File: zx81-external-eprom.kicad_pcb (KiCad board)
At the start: 2 copper layers, 60.3 x 50 mm, 11 parts, among them J1 Connector ZX81, Q1 BC549, SW1 ROM select, U1 W27C512, U2 74LS138

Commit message: cosmetic changes
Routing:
- added copper zone on F.Cu, net GND
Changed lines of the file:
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@@
 		)
 		(property "Value" "ROM select"
-			(at 3.77 9.2 270)
+			(at 3.77 9.2 -90)
 			(layer "F.SilkS")
 			(effects
@@
 	)
 	(zone
+		(net 21)
+		(net_name "GND")
+		(layer "F.Cu")
+		(hatch edge 0.5)
+		(connect_pads
+			(clearance 0.5)
+		)
+		(min_thickness 0.25)
+		(filled_areas_thickness no)
+		(fill yes
+			(thermal_gap 0.5)
+			(thermal_bridge_width 0.5)
+		)
+		(polygon
+			(pts
+				(xy 107.45 37.97) (xy 47.71 37.97) (xy 47.71 79.11) (xy 107.46 79.12)
+			)
+		)
+	)
+	(zone

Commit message: Local SYMBOL & FOOTPRINT
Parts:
- G200: footprint ZXINFO:ZXInfo_kicad_logo_copper_16.5x5 -> ZXINFO_FOOTPRINT:ZXInfo_kicad_logo_copper_16.5x5
- J1: footprint ZXINFO:EDGE ZX81_1 -> ZXINFO_FOOTPRINT:EDGE ZX81 BOTTOM
- SW1: value ROM select -> SW_DIP_x03
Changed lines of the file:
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@@
 		)
 	)
-	(footprint "ZXINFO:EDGE ZX81_1"
+	(footprint "ZXINFO_FOOTPRINT:EDGE ZX81 BOTTOM"
 		(layer "F.Cu")
 		(at 78.9246 83.68)
@@
 			)
 		)
-		(property "Footprint" "ZXINFO:EDGE ZX81_1"
+		(property "Footprint" "ZXINFO_FOOTPRINT:EDGE ZX81 BOTTOM"
 			(at -5.104618 2.54 180)
 			(unlocked yes)
@@
 			)
 		)
+		(property ki_fp_filters "SINCLAIR:ZX_*")
+		(sheetname "Root")
+		(sheetfile "zx81-external-eprom.kicad_sch")
 		(attr through_hole)
-		(fp_text user "A0"
-			(at -14.187654 -4.530952 -90)
+		(fp_text user "A9"
+			(at 11.2 -4.530952 -90)
 			(unlocked yes)
 			(layer "B.SilkS")
@@
 			)
 		)
-		(fp_text user "A8"
-			(at 13.762365 -4.530952 -90)
+		(fp_text user "GND"
+			(at -19.237654 -4.530952 -90)
 			(unlocked yes)
 			(layer "B.SilkS")
@@
 			)
 		)
-		(fp_text user "+9V"
-			(at -26.887654 -4.530952 -90)
+		(fp_text user "A10"
+			(at 8.75 -4.530952 -90)
 			(unlocked yes)
 			(layer "B.SilkS")
@@
 			)
 		)
-		(fp_text user "A11"
-			(at 5.962365 -4.530952 -90)
+		(fp_text user "A2"
+			(at -9.137654 -4.530952 -90)
 			(unlocked yes)
 			(layer "B.SilkS")
@@
 			)
 		)
-		(fp_text user "SLOT"
-			(at 19 2.1 90)
+		(fp_text user "CLK"
+			(at -16.687654 -4.530952 -90)
 			(unlocked yes)
 			(layer "B.SilkS")
-			(hide yes)
 			(effects
 				(font
@@
 			)
 		)
-		(fp_text user "A9"
-			(at 11.2 -4.530952 -90)
+		(fp_text user "A15"
+			(at -4.087654 -4.530952 -90)
 			(unlocked yes)
 			(layer "B.SilkS")
@@
 			)
 		)
-		(fp_text user "CLK"
-			(at -16.687654 -4.530952 -90)
+		(fp_text user "A8"
+			(at 13.762365 -4.530952 -90)
 			(unlocked yes)
 			(layer "B.SilkS")
@@
 			)
 		)
-		(fp_text user "A15"
-			(at -4.087654 -4.530952 -90)
+		(fp_text user "SLOT"
+			(at 19 2.1 90)
 			(unlocked yes)
 			(layer "B.SilkS")
+			(hide yes)
 			(effects
 				(font
@@
 			)
 		)
-		(fp_text user "A6"
-			(at 18.741358 -4.530952 -90)
+		(fp_text user "A1"
+			(at -11.587654 -4.530952 -90)
 			(unlocked yes)
 			(layer "B.SilkS")
@@
 			)
 		)
-		(fp_text user "~{ROMCS}"
-			(at 26.65 -4.530952 -90)
+		(fp_text user "A13"
+			(at 0.855556 -4.530952 -90)
 			(unlocked yes)
 			(layer "B.SilkS")
@@
 			)
 		)
-		(fp_text user "A14"
-			(at -1.387654 -4.530952 -90)
+		(fp_text user "A11"
+			(at 5.962365 -4.530952 -90)
 			(unlocked yes)
 			(layer "B.SilkS")
@@
 			)
 		)
-		(fp_text user "A2"
-			(at -9.137654 -4.530952 -90)
+		(fp_text user "A12"
+			(at 3.512365 -4.530952 -90)
 			(unlocked yes)
 			(layer "B.SilkS")
@@
 			)
 		)
-		(fp_text user "A10"
-			(at 8.75 -4.530952 -90)
+		(fp_text user "A7"
+			(at 16.248148 -4.530952 -90)
 			(unlocked yes)
 			(layer "B.SilkS")
@@
 			)
 		)
-		(fp_text user "+5V"
-			(at -29.537654 -4.530952 -90)
+		(fp_text user "+9V"
+			(at -26.887654 -4.530952 -90)
 			(unlocked yes)
 			(layer "B.SilkS")
@@
 			)
 		)
-		(fp_text user "A13"
-			(at 0.855556 -4.530952 -90)
+		(fp_text user "A0"
+			(at -14.187654 -4.530952 -90)
 			(unlocked yes)
 			(layer "B.SilkS")
@@
 			)
 		)
-		(fp_text user "A1"
-			(at -11.587654 -4.530952 -90)
+		(fp_text user "+5V"
+			(at -29.537654 -4.530952 -90)
 			(unlocked yes)
 			(layer "B.SilkS")
@@
 			)
 		)
-		(fp_text user "GND"
-			(at -21.837654 -4.530952 -90)
+		(fp_text user "A6"
+			(at 18.741358 -4.530952 -90)
 			(unlocked yes)
 			(layer "B.SilkS")
@@
 			)
 		)
-		(fp_text user "A7"
-			(at 16.248148 -4.530952 -90)
+		(fp_text user "A14"
+			(at -1.387654 -4.530952 -90)
 			(unlocked yes)
 			(layer "B.SilkS")
@@
 			)
 		)
-		(fp_text user "A12"
-			(at 3.512365 -4.530952 -90)
+		(fp_text user "GND"
+			(at -21.837654 -4.530952 -90)
 			(unlocked yes)
 			(layer "B.SilkS")
@@
 			)
 		)
-		(fp_text user "GND"
-			(at -19.237654 -4.530952 -90)
+		(fp_text user "A4"
+			(at 23.727778 -4.530952 -90)
 			(unlocked yes)
 			(layer "B.SilkS")
@@
 			)
 		)
-		(fp_text user "A4"
-			(at 23.727778 -4.530952 -90)
+		(fp_text user "~{ROMCS}"
+			(at 26.65 -4.530952 -90)
 			(unlocked yes)
 			(layer "B.SilkS")
@@
 			)
 		)
-		(fp_text user "D2"
-			(at -16.780546 -4.530952 90)
+		(fp_text user "D4"
+			(at -6.780546 -4.530952 90)
 			(unlocked yes)
 			(layer "F.SilkS")
@@
 			)
 		)
-		(fp_text user "D0"
-			(at -21.830546 -4.530952 90)
+		(fp_text user "D2"
+			(at -16.780546 -4.530952 90)
 			(unlocked yes)
 			(layer "F.SilkS")
@@
 			)
 		)
-		(fp_text user "D5"
-			(at -11.703386 -4.530952 90)
+		(fp_text user "~{INT}"
+			(at -3.875928 -4.530952 90)
 			(unlocked yes)
 			(layer "F.SilkS")
@@
 			)
 		)
-		(fp_text user "~{WAIT}"
-			(at 16.624072 -4.530952 90)
+		(fp_text user "~{RESET}"
+			(at 21.462346 -4.530952 90)
 			(unlocked yes)
 			(layer "F.SilkS")
@@
 			)
 		)
-		(fp_text user "~{RAMCS}"
-			(at -26.775928 -4.530952 90)
+		(fp_text user "~{M1}"
+			(at 23.962346 -4.530952 90)
 			(unlocked yes)
 			(layer "F.SilkS")
@@
 			)
 		)
-		(fp_text user "~{M1}"
-			(at 23.962346 -4.530952 90)
+		(fp_text user "D1"
+			(at -19.280546 -4.530952 90)
 			(unlocked yes)
 			(layer "F.SilkS")
@@
 			)
 		)
-		(fp_text user "~{NMI}"
-			(at -1.225928 -4.530952 90)
+		(fp_text user "~{MREQ}"
+			(at 3.712346 -4.530952 90)
 			(unlocked yes)
 			(layer "F.SilkS")
@@
 			)
 		)
-		(fp_text user "D7"
-			(at -29.430546 -4.530952 90)
+		(fp_text user "~{WAIT}"
+			(at 16.624072 -4.530952 90)
 			(unlocked yes)
 			(layer "F.SilkS")
@@
 			)
 		)
-		(fp_text user "D6"
-			(at -14.260176 -4.530952 90)
+		(fp_text user "D5"
+			(at -11.703386 -4.530952 90)
 			(unlocked yes)
 			(layer "F.SilkS")
@@
 			)
 		)
-		(fp_text user "~{RFSH}"
-			(at 26.512346 -4.530952 90)
+		(fp_text user "~{HALT}"
+			(at 1.024072 -4.530952 90)
 			(unlocked yes)
 			(layer "F.SilkS")
@@
 			)
 		)
-		(fp_text user "D4"
-			(at -6.780546 -4.530952 90)
+		(fp_text user "D0"
+			(at -21.830546 -4.530952 90)
 			(unlocked yes)
 			(layer "F.SilkS")
@@
 			)
 		)
-		(fp_text user "~{MREQ}"
-			(at 3.712346 -4.530952 90)
+		(fp_text user "~{NMI}"
+			(at -1.225928 -4.530952 90)
 			(unlocked yes)
 			(layer "F.SilkS")
@@
 			)
 		)
-		(fp_text user "~{RESET}"
-			(at 21.462346 -4.530952 90)
+		(fp_text user "~{RD}"
+			(at 8.712346 -4.530952 90)
 			(unlocked yes)
 			(layer "F.SilkS")
@@
 			)
 		)
-		(fp_text user "~{WR}"
-			(at 11.262346 -4.530952 90)
+		(fp_text user "D7"
+			(at -29.430546 -4.530952 90)
 			(unlocked yes)
 			(layer "F.SilkS")
@@
 			)
 		)
-		(fp_text user "~{BUSRQ}"
-			(at 18.874072 -4.530952 90)
+		(fp_text user "~{RFSH}"
+			(at 26.512346 -4.530952 90)
 			(unlocked yes)
 			(layer "F.SilkS")
@@
 			)
 		)
-		(fp_text user "D1"
-			(at -19.280546 -4.530952 90)
+		(fp_text user "~{RAMCS}"
+			(at -26.775928 -4.530952 90)
 			(unlocked yes)
 			(layer "F.SilkS")
@@
 			)
 		)
-		(fp_text user "~{RD}"
-			(at 8.712346 -4.530952 90)
+		(fp_text user "SLOT"
+			(at -24.204618 0.64 90)
 			(unlocked yes)
 			(layer "F.SilkS")
+			(hide yes)
 			(effects
 				(font
@@
 			)
 		)
-		(fp_text user "~{HALT}"
-			(at 1.024072 -4.530952 90)
+		(fp_text user "~{BUSRQ}"
+			(at 18.874072 -4.530952 90)
 			(unlocked yes)
 			(layer "F.SilkS")
@@
 			)
 		)
-		(fp_text user "SLOT"
-			(at -24.204618 0.64 90)
+		(fp_text user "~{WR}"
+			(at 11.262346 -4.530952 90)
 			(unlocked yes)
 			(layer "F.SilkS")
-			(hide yes)
 			(effects
 				(font
@@
 			)
 		)
-		(fp_text user "~{INT}"
-			(at -3.875928 -4.530952 90)
+		(fp_text user "D6"
+			(at -14.260176 -4.530952 90)
 			(unlocked yes)
 			(layer "F.SilkS")
@@
 			)
 		)
-		(property "Value" "ROM select"
+		(property "Value" "SW_DIP_x03"
 			(at 3.77 9.2 -90)
 			(layer "F.SilkS")
@@
 		)
 	)
-	(footprint "ZXINFO:ZXInfo_kicad_logo_copper_16.5x5"
+	(footprint "ZXINFO_FOOTPRINT:ZXInfo_kicad_logo_copper_16.5x5"
 		(layer "B.Cu")
 		(at 83.471884 42.638103 180)

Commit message: small design fixes
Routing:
- net Net-(J1-~{MREQ}): track 57.3 -> 76.5 mm
- net D1: track 45.5 -> 33.2 mm, vias 0 -> 1
- net A7: track 39.4 -> 47.6 mm
- net Net-(J1-~{RFSH}): track 83.0 -> 74.8 mm
- net A4: track 55.3 -> 48.1 mm, vias 0 -> 1
- net D0: track 39.3 -> 32.4 mm, vias 0 -> 1
- net +5V: track 112.3 -> 106.7 mm, vias 0 -> 1
- net A6: track 45.7 -> 40.4 mm
- net Net-(J1-~{RD}): track 64.2 -> 60.8 mm
- net A5: track 51.0 -> 47.7 mm
- net A3: track 33.0 -> 36.1 mm, vias 0 -> 1
- net D7: track 27.6 -> 29.8 mm, vias 1 -> 0
- net Net-(U1-A15): track 36.7 -> 38.5 mm
- net D2: track 36.8 -> 35.5 mm
- net A15: track 48.6 -> 47.4 mm, vias 1 -> 0
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- removed copper zone on B.Cu, net GND
- removed copper zone on F.Cu, net GND

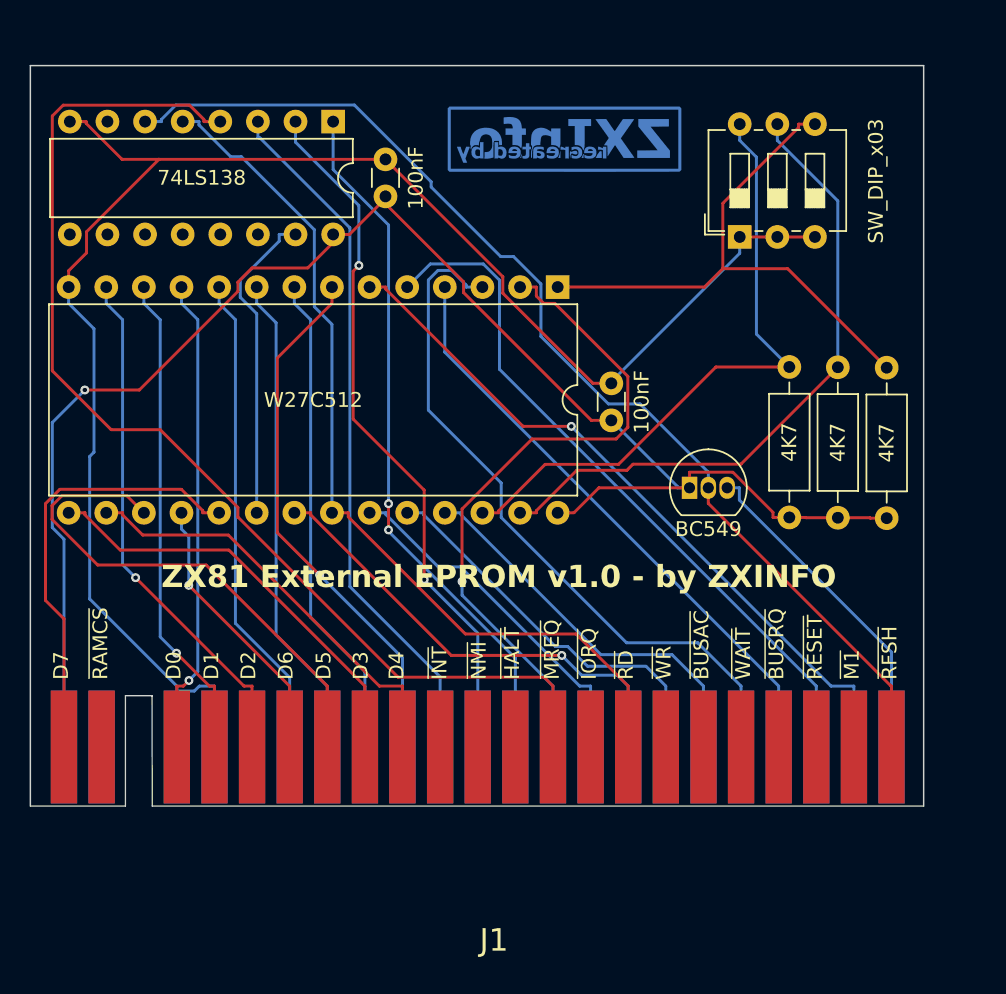
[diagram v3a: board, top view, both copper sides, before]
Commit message: changed Resistor to 10K
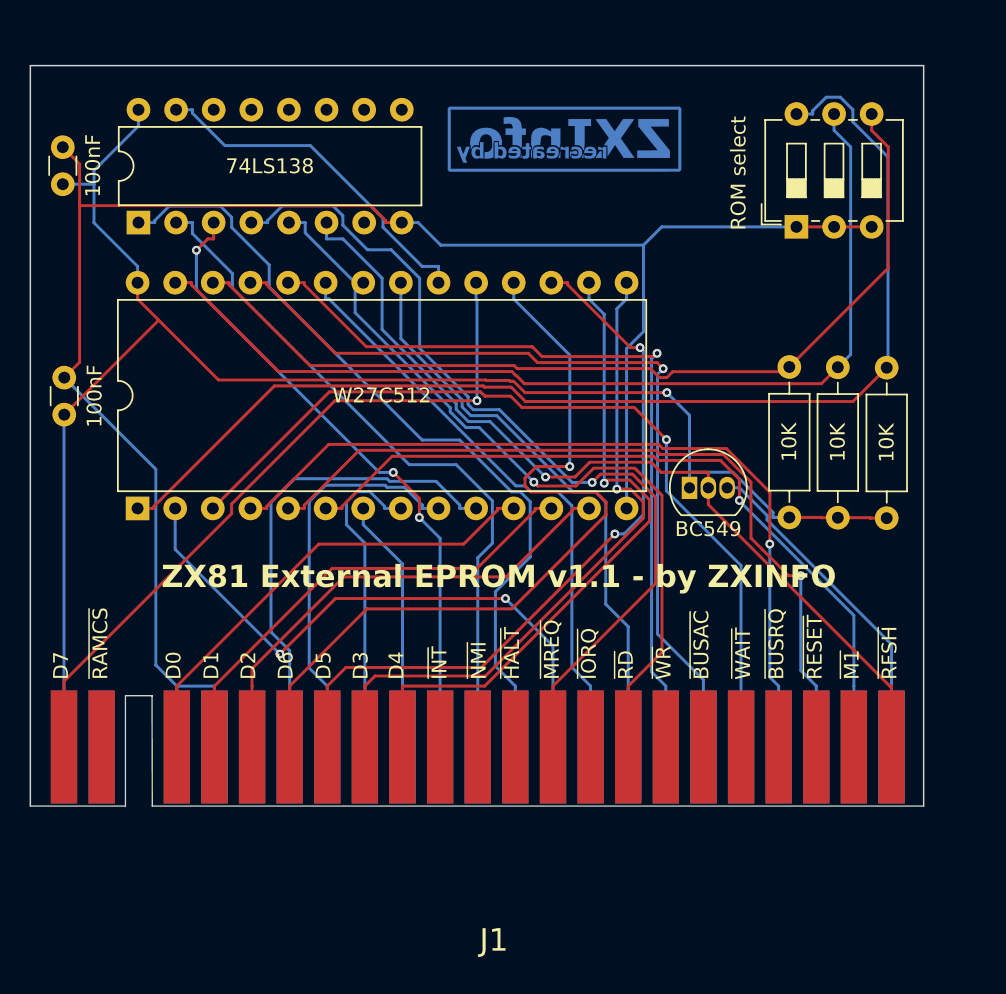
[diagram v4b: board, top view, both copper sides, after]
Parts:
- R1, R2, R3: value 4K7 -> 10K
- moved C1 36.9 mm to (49.7, 61.2)
- moved U1 32.1 mm to (54.7, 67.6), turned to 90 degrees
- moved C2 21.8 mm to (49.6, 45.7)
- moved U2 14.8 mm to (54.7, 48.3), turned to 90 degrees
- moved SW1 3.89 mm to (99.2, 48.6)
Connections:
- SW1 pad 4: Net-(U1-A15) -> Net-(U1-A13)
- SW1 pad 6: Net-(U1-A13) -> Net-(U1-A15)
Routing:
- net Net-(U1-A15): track 38.5 -> 78.7 mm
- net D6: track 18.8 -> 54.9 mm
- net A8: track 26.5 -> 57.3 mm, vias 0 -> 1
- net A9: track 26.5 -> 54.3 mm, vias 0 -> 1
- net Net-(U1-A14): track 43.7 -> 66.0 mm
- net Net-(U1-A13): track 42.7 -> 62.3 mm
- net A3: track 36.1 -> 17.2 mm, vias 1 -> 0
- net D7: track 29.8 -> 48.5 mm, vias 0 -> 1
- net Net-(J1-~{MREQ}): track 76.5 -> 59.6 mm, vias 0 -> 1
- net A11: track 24.0 -> 40.3 mm
- net D3: track 29.0 -> 45.0 mm, vias 0 -> 1
- net D4: track 29.0 -> 44.5 mm, vias 0 -> 1
- net A6: track 40.4 -> 55.7 mm, vias 0 -> 1
- net Net-(J1-~{RFSH}): track 74.8 -> 60.2 mm, vias 0 -> 1
- net D5: track 35.2 -> 49.5 mm, vias 0 -> 2
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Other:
- board text added: "ROM select"
- board text added: "ZX81 External EPROM v1.1 - by ZXINFO"
- board text removed: "ZX81 External EPROM v1.0 - by ZXINFO"

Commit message: version 1.2
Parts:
- removed G200: LOGO, ZXINFO_FOOTPRINT:ZXInfo_kicad_logo_copper_16.5x5
- removed SW1: SW_DIP_x03, Button_Switch_THT:SW_DIP_SPSTx03_Slide_6.7x9.18mm_W7.62mm_P2.54mm_LowProfile
- added C3: 100nF, Capacitor_THT:C_Disc_D3.0mm_W1.6mm_P2.50mm, F.Cu at (71.4, 37.4)
- added R4: 4K7, Resistor_THT:R_Axial_DIN0207_L6.3mm_D2.5mm_P10.16mm_Horizontal, F.Cu at (105.6, 52.9)
- added SW2: SW_DIP_x04, Button_Switch_THT:SW_DIP_SPSTx04_Slide_6.7x11.72mm_W7.62mm_P2.54mm_LowProfile, F.Cu at (97.1, 47.2)
- added U3: 74LS157, Package_DIP:DIP-16_W7.62mm, F.Cu at (72.0, 47.3)
- moved R3 11.6 mm to (94.8, 52.9)
- moved C1 10.7 mm to (49.1, 50.6), turned to 0 degrees
- moved C2 8.32 mm to (49.2, 37.4), turned to 0 degrees
- moved R2 6.26 mm to (98.4, 52.9)
- moved R1 6.12 mm to (102.0, 52.9)
- moved Q1 5.42 mm to (90.1, 61.1), turned to 180 degrees
- moved U2 5.16 mm to (49.6, 47.3)
- moved U1 5.06 mm to (49.6, 68.1)
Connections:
- J1 pad A15: A13 -> Net-(J1-A13)
- R1 pad 1: Net-(U1-A13) -> Net-(U3-I0b)
- R1 pad 2: +5V -> GND
- R2 pad 2: +5V -> GND
- R3 pad 2: +5V -> GND
- U2 pad 1: A13 -> Net-(U2-A0)
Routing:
- net A13: track 54.6 -> 0.00 mm
- net Net-(U3-S): track 0.00 -> 49.9 mm
- net Net-(J1-A13): track 0.00 -> 49.4 mm
- net Net-(U3-I0b): track 0.00 -> 40.8 mm
- net GND: track 124.6 -> 164.0 mm
- net Net-(U2-A0): track 0.00 -> 32.0 mm
- net Net-(U1-A13): track 62.3 -> 34.9 mm
- net D6: track 54.9 -> 35.7 mm
- net +5V: track 109.0 -> 126.3 mm, vias 1 -> 0
- net D5: track 49.5 -> 35.4 mm, vias 2 -> 1
- net A0: track 32.5 -> 19.1 mm, vias 0 -> 1
- net Net-(U1-A15): track 78.7 -> 65.8 mm
- net A1: track 27.0 -> 16.0 mm, vias 0 -> 1
- net Net-(J1-~{MREQ}): track 59.6 -> 48.8 mm
- net Net-(J1-~{RFSH}): track 60.2 -> 69.3 mm, vias 1 -> 0
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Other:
- board size 60.3 x 50 mm -> 60.3 x 52.4 mm
- board text added: "16/8K"
- board text added: "A15A14A13"
- board text added: "JLCJLCJLCJLC"
- board text added: "ZX81 External EPROM v1.2 - by ZXINFO"
- board text removed: "ZX81 External EPROM v1.1 - by ZXINFO"
